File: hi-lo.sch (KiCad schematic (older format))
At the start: 25 parts, among them U31 TC4427, U32 TC4427, U33 TC4427

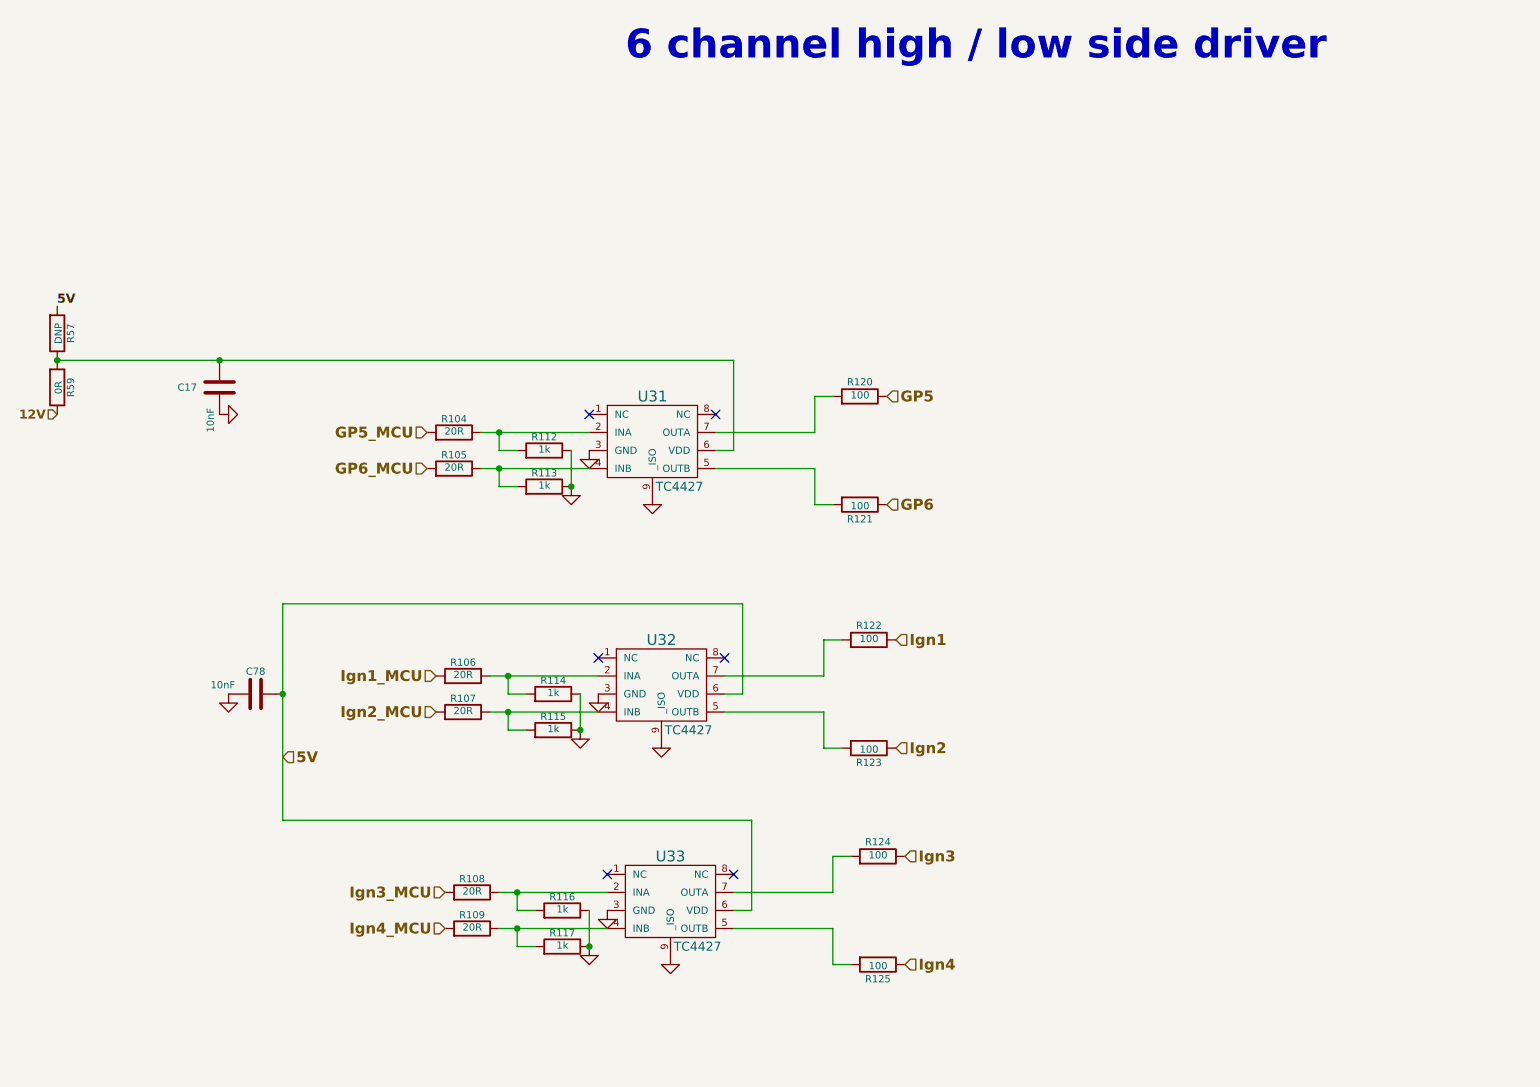
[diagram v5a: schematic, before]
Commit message: Significant revision of schematic and layout:
Added reverse voltage protection.
Split 12V supply into a 12V-Key (ignition) pin and a 12V-MRel (supply from
main relay) pin.  The 12V main relay is controlled by the MRel pin to protect against reverse voltage and over-voltage.

The board can optionally draw under 1mA from the main relay coil to power
standby features, including CAN monitoring.

Increased the size of several resistors, notably ignition output resistors
and CAN termination, to handle typical power draw.

Changed resistor dividers to individual resistors for better accuracy than
typical resistor networks.

Standardized pull-up and pull-down resistors to 10K.

Changed to a tab-output regulator.
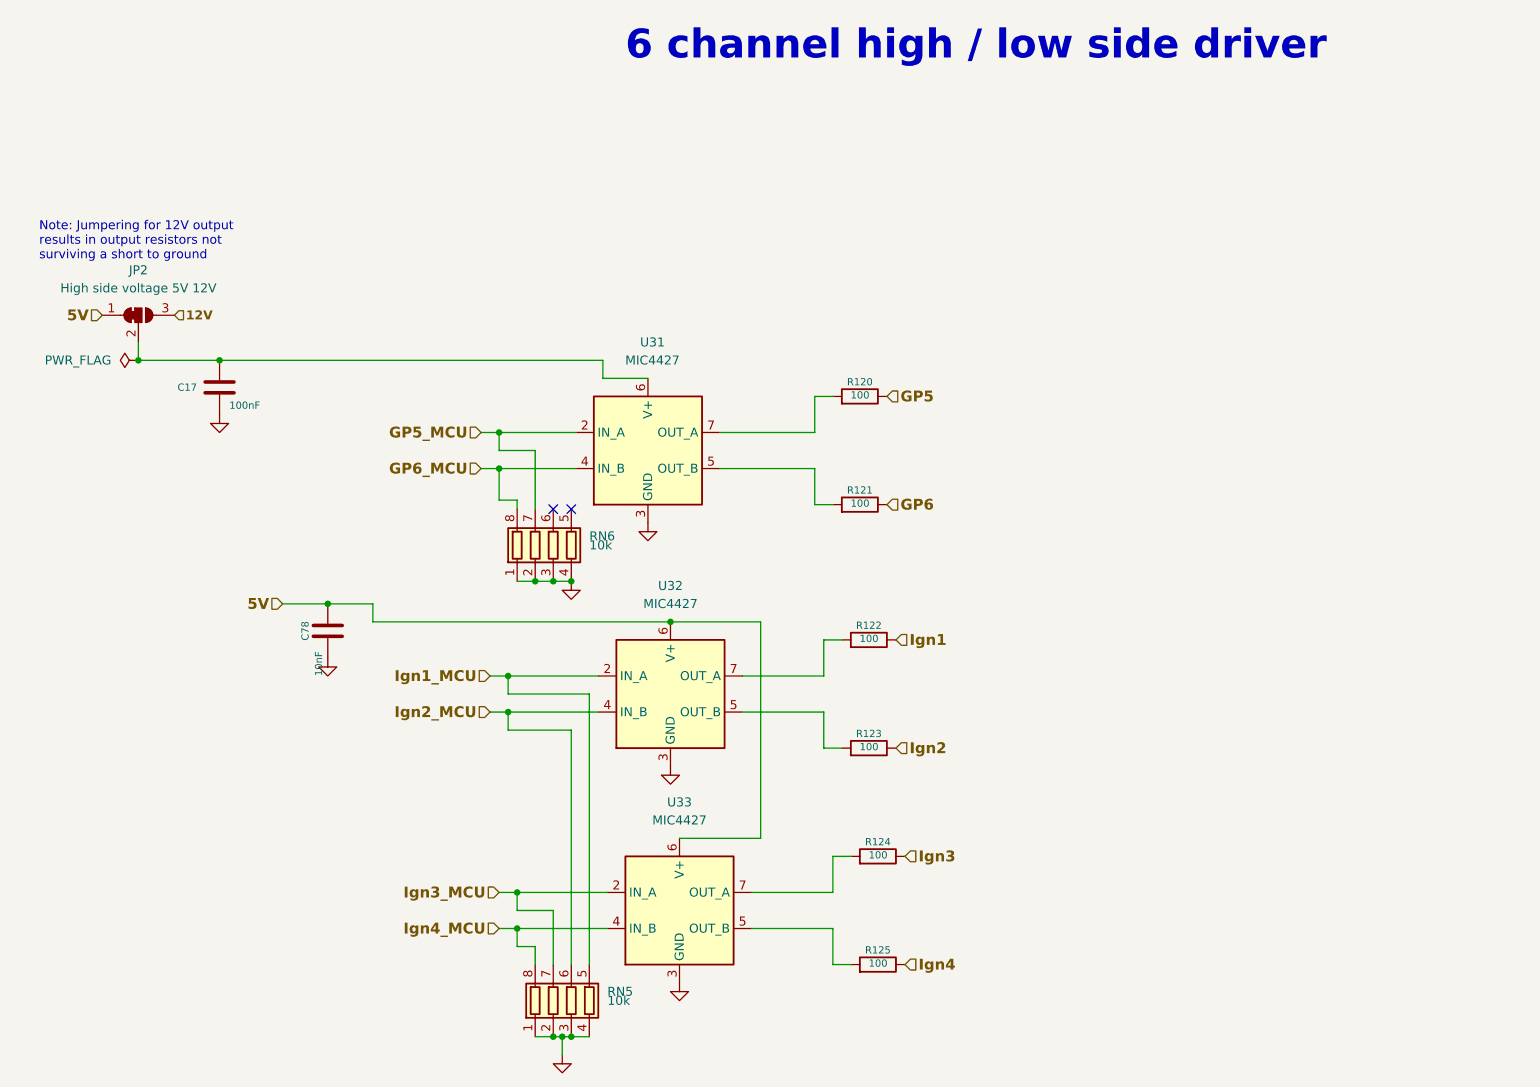
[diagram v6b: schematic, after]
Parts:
- removed R104, R105, R106, R107, R108, R109: 20R, Resistor_SMD:R_0603_1608Metric, symbol Device:R
- removed R112, R113, R114, R115, R116, R117: 1k, Resistor_SMD:R_0603_1608Metric, symbol Device:R
- removed R57: DNP, Resistor_SMD:R_0603_1608Metric, symbol Device:R
- removed R59: 0R, Resistor_SMD:R_0603_1608Metric, symbol Device:R
- removed U31, U32, U33: TC4427, modules:DFN-8-1EP_6x5mm_P1.27mm_EP4x2mm, symbol rusefi_tc4427:TC4427
- added JP2: High side voltage 5V 12V, Jumper:SolderJumper-3_P1.3mm_Bridged2Bar12_Pad1.0x1.5mm, symbol Jumper:SolderJumper_3_Bridged12
- added RN5, RN6: 10k, Resistor_SMD:R_Array_Convex_4x0603, symbol Device:R_Pack04
- added U31, U32, U33: MIC4427, Package_SO:SOIC-8_3.9x4.9mm_P1.27mm, symbol Driver_FET:MIC4427
- C17: value 10nF -> 100nF; LCSC (none) -> C14663; Manufacturer KEMET -> (none); Part # C0603C103K1RACTU -> (none); VEND DIGI -> (none); VEND# 399-3189-1-ND -> (none)
- C78: LCSC (none) -> C57112
- R120, R121, R122, R123, R124, R125: footprint Resistor_SMD:R_0603_1608Metric -> Resistor_SMD:R_1206_3216Metric; LCSC (none) -> C17901
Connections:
- net 12V: now also JP2.3 (B)
- net 5V: now also JP2.1 (A), U32.6 (V+), U33.6 (V+)
- net GND: now also RN5.1 (R1.1), RN5.2 (R2.1), RN5.3 (R3.1), RN5.4 (R4.1), RN6.1 (R1.1), RN6.2 (R2.1), RN6.3 (R3.1), RN6.4 (R4.1), U31.3 (GND), U32.3 (GND), U33.3 (GND)
- net GP5_MCU: now also RN6.7 (R2.2), U31.2 (IN_A)
- net GP6_MCU: now also RN6.8 (R1.2), U31.4 (IN_B)
- net Ign1_MCU: now also RN5.5 (R4.2), U32.2 (IN_A)
- net Ign2_MCU: now also RN5.6 (R3.2), U32.4 (IN_B)
- net Ign3_MCU: now also RN5.7 (R2.2), U33.2 (IN_A)
- net Ign4_MCU: now also RN5.8 (R1.2), U33.4 (IN_B)
- net at R125.2: now also U33.5 (OUT_B)
- net at R124.2: now also U33.7 (OUT_A)
- net at R123.2: now also U32.5 (OUT_B)
- net at R122.2: now also U32.7 (OUT_A)
- net at R121.2: now also U31.5 (OUT_B)
- net at R120.2: now also U31.7 (OUT_A)
- net at C17.1: now also JP2.2 (C), U31.6 (V+)
- no-connect marks 6 -> 2
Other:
- note added: "Note: Jumpering for 12V output\nresults in output resistors not\nsurviving a short to ground"
- moved on the sheet: C78

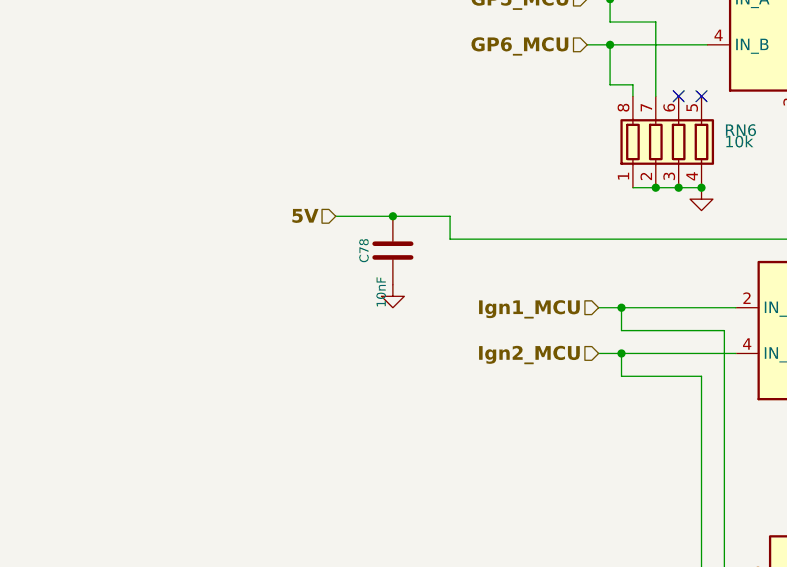
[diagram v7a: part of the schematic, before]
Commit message: Added 2x5 header for SPI/serial communications Connected LIN to PD8/PD9 USART3, output on SMD testpoint. Added standby regulator. Changed footprints of reverse protection diodes to SMA. Rotated two opamps and clamping diode arrays for cleaner layout. Moved status LEDs over for better silkscreen labels. Moved CAN termination and TVS to lower right.
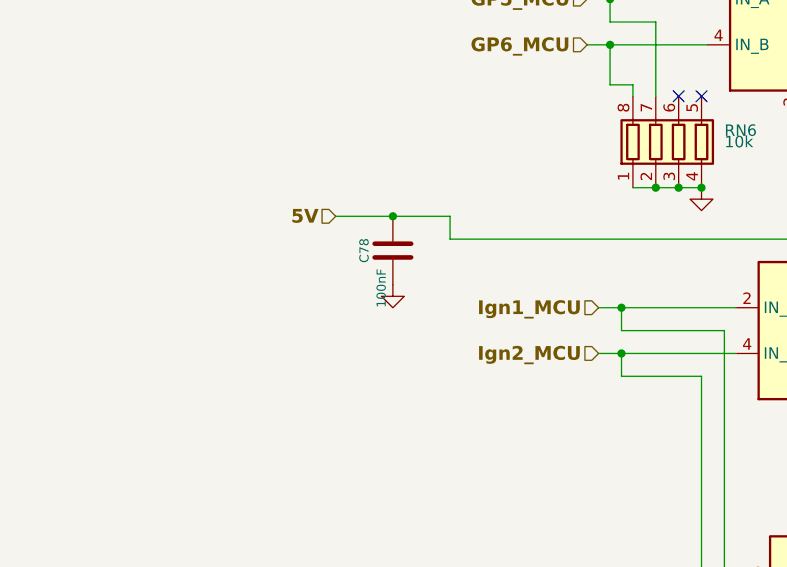
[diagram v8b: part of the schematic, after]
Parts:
- C78: value 10nF -> 100nF; LCSC C57112 -> C14663; Manufacturer KEMET -> (none); Part # C0603C103K1RACTU -> (none); VEND DIGI -> (none); VEND# 399-3189-1-ND -> (none)
- U31, U32, U33: LCSC (none) -> C144205
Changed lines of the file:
@@
 $Descr B 17000 11000
 encoding utf-8
-Sheet 3 7
-Title "microRusEfi"
-Date "2019-09-24"
-Rev "R0.4.2"
+Sheet 2 7
+Title "microRusEfi-2L"
+Date "2019-10-06"
+Rev "R0.4.5"
 Comp "rusEFI.com"
-Comment1 ""
+Comment1 "Donald Becker"
 Comment2 ""
 Comment3 ""
@@
 P 4600 6450
 F 0 "C78" V 4725 6450 40  0000 C CNN
-F 1 "10nF" V 4650 6200 40  0000 L CNN
+F 1 "100nF" V 4650 6200 40  0000 L CNN
 F 2 "Capacitor_SMD:C_0603_1608Metric" V -1720 1500 60  0001 C CNN
 F 3 "" H 4600 6450 60  0001 C CNN
-F 4 "C0603C103K1RACTU" H 400 -350 50  0001 C CNN "Part #"
-F 5 "DIGI" H 400 -350 50  0001 C CNN "VEND"
-F 6 "399-3189-1-ND" H 400 -350 50  0001 C CNN "VEND#"
-F 7 "KEMET" H 400 -350 50  0001 C CNN "Manufacturer"
-F 8 "C57112" H 4600 6450 50  0001 C CNN "LCSC"
+F 4 "C14663" H 4600 6450 50  0001 C CNN "LCSC"
 	1    4600 6450
 	-1   0    0    -1
@@
 F 2 "Package_SO:SOIC-8_3.9x4.9mm_P1.27mm" H 6375 5150 50  0001 C CNN
 F 3 "http://ww1.microchip.com/downloads/en/DeviceDoc/mic4426.pdf" H 6375 5150 50  0001 C CNN
+F 4 "C144205" H 6375 5450 50  0001 C CNN "LCSC"
 	1    6375 5450
 	1    0    0    -1
@@
 F 2 "Package_SO:SOIC-8_3.9x4.9mm_P1.27mm" H 6550 7700 50  0001 C CNN
 F 3 "http://ww1.microchip.com/downloads/en/DeviceDoc/mic4426.pdf" H 6550 7700 50  0001 C CNN
+F 4 "C144205" H 6550 8000 50  0001 C CNN "LCSC"
 	1    6550 8000
 	1    0    0    -1
@@
 F 2 "Package_SO:SOIC-8_3.9x4.9mm_P1.27mm" H 6500 6500 50  0001 C CNN
 F 3 "http://ww1.microchip.com/downloads/en/DeviceDoc/mic4426.pdf" H 6500 6500 50  0001 C CNN
+F 4 "C144205" H 6500 6800 50  0001 C CNN "LCSC"
 	1    6500 6800
 	1    0    0    -1
